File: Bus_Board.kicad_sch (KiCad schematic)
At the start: 44 parts, among them J1 +5V, J10 Conn_02x05_Odd_Even, J11 Conn_02x08_Odd_Even, J12 Conn_02x05_Odd_Even, J13 Conn_02x08_Odd_Even, J14 Conn_02x05_Odd_Even, J15 Conn_02x08_Odd_Even, J16 Conn_02x05_Odd_Even, J17 Conn_02x08_Odd_Even, J18 Conn_02x05_Odd_Even, J19 Conn_02x08_Odd_Even, J2 +12V, J20 Conn_02x05_Odd_Even, J21 Conn_02x08_Odd_Even, J22 Conn_02x05_Odd_Even, J23 Conn_02x08_Odd_Even, J24 Conn_02x05_Odd_Even, J25 +5V, J26 +12V, J27 GND, J28 -12V, J3 GND, J4 -12V, J5 Conn_02x08_Odd_Even, J6 Conn_02x05_Odd_Even, J7 Conn_02x08_Odd_Even, J8 Conn_02x05_Odd_Even, J9 Conn_02x08_Odd_Even

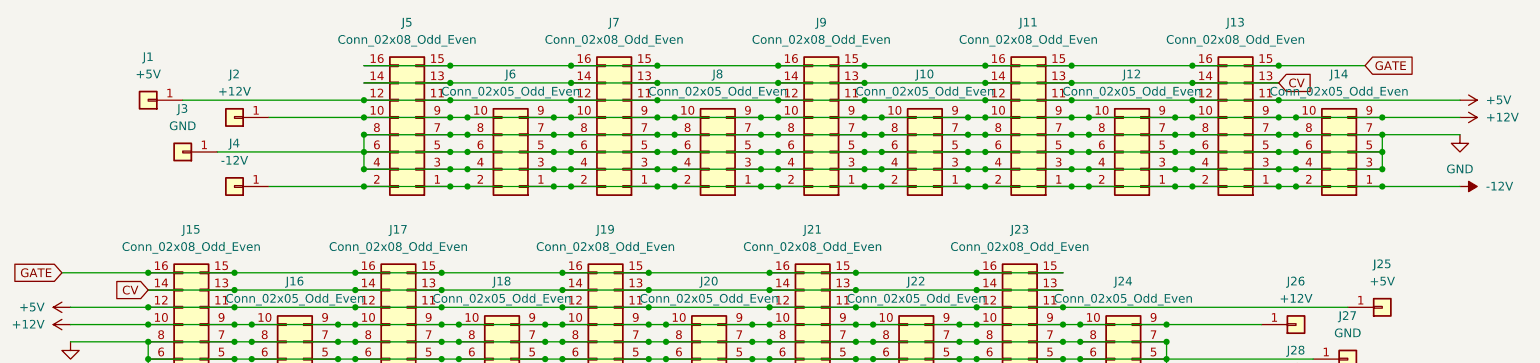
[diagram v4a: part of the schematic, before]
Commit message: Add schematic pdf
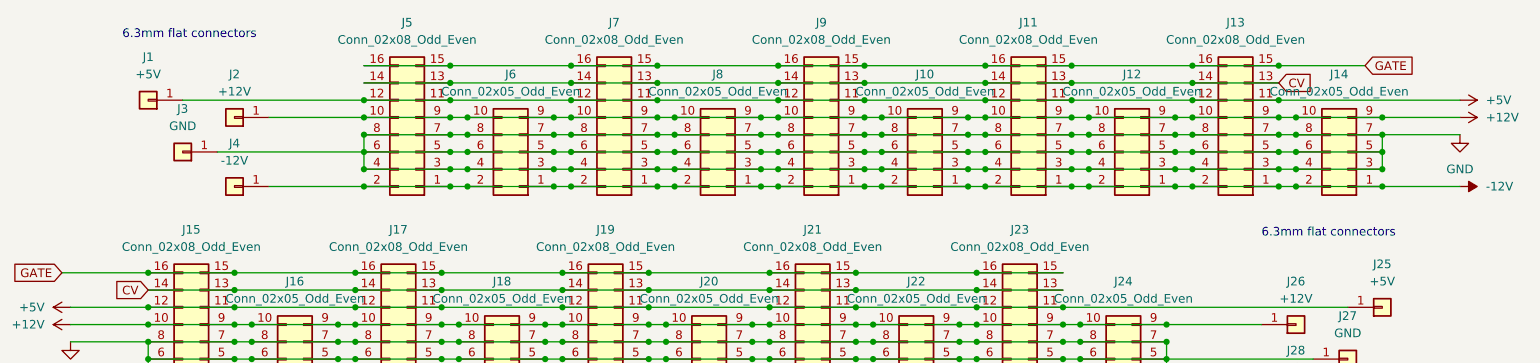
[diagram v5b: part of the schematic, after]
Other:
- note added: "6.3mm flat connectors"
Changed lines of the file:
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@@
     (stroke (width 0) (type default) (color 0 0 0 0))
+  )
+  (text "6.3mm flat connectors" (at 52.07 36.83 0)
+    (effects (font (size 1.27 1.27)) (justify left bottom))
+  )
+  (text "6.3mm flat connectors" (at 219.71 66.04 0)
+    (effects (font (size 1.27 1.27)) (justify left bottom))
   )
   (global_label "CV" (shape input) (at 222.25 43.18 0) (fields_autoplaced)
